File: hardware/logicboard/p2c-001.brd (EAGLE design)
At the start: 91 x 55 mm, 49 parts, among them IC1 74LS07N, J1 POWER_JACKSLT, J2 RLY, J3 DISP, J4 PWR, J5 DIN5, J6 DIN5, J7 Qwiic, K1 G5V1, Q1 220mA/50V/3.5Ω, Q2 220mA/50V/3.5Ω, SW1 A6A-16R, T1 2SC1815, U1 DS18B20

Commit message: Fixed value of capacitor.
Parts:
- C2: value 0.47u -> 0.33u
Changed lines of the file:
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@@
 <?xml version="1.0" encoding="utf-8"?>
 <!DOCTYPE eagle SYSTEM "eagle.dtd">
-<eagle version="9.5.2">
+<eagle version="9.6.1">
 <drawing>
 <settings>
@@
 <attribute name="VALUE" x="30.222" y="10.333" size="1.27" layer="27" ratio="10"/>
 </element>
-<element name="C2" library="rcl" library_urn="urn:adsk.eagle:library:334" package="C050-024X044" package3d_urn="urn:adsk.eagle:package:23643/1" value="0.47u" x="24" y="13" smashed="yes">
+<element name="C2" library="rcl" library_urn="urn:adsk.eagle:library:334" package="C050-024X044" package3d_urn="urn:adsk.eagle:package:23643/1" value="0.33u" x="24" y="13" smashed="yes">
 <attribute name="NAME" x="20.5" y="13" size="1" layer="25" ratio="10" rot="R90" align="bottom-center"/>
 <attribute name="POPULARITY" value="33" x="24" y="13" size="1.778" layer="27" display="off"/>

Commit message: Renamed J7 to JQ1.
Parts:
- renumbered J7 to JQ1
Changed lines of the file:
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@@
 <?xml version="1.0" encoding="utf-8"?>
 <!DOCTYPE eagle SYSTEM "eagle.dtd">
-<eagle version="9.6.1">
+<eagle version="9.5.2">
 <drawing>
 <settings>
@@
 <attribute name="VALUE" x="61.8664" y="30.2286" size="0.9906" layer="27" ratio="10"/>
 </element>
-<element name="J7" library="SparkFun-Connectors" library_urn="urn:adsk.eagle:library:513" package="1X04_1MM_RA" package3d_urn="urn:adsk.eagle:package:38096/1" value="Qwiic" x="45.5" y="49" smashed="yes" rot="MR180">
+<element name="JQ1" library="SparkFun-Connectors" library_urn="urn:adsk.eagle:library:513" package="1X04_1MM_RA" package3d_urn="urn:adsk.eagle:package:38096/1" value="Qwiic" x="45.5" y="49" smashed="yes" rot="MR180">
 <attribute name="NAME" x="45.5" y="47" size="1" layer="26" ratio="20" rot="MR0" align="bottom-center"/>
 <attribute name="VALUE" x="43.849" y="52.302" size="0.6096" layer="28" font="vector" ratio="20" rot="MR180"/>
@@
 <contactref element="C5" pad="2"/>
 <contactref element="C6" pad="2"/>
-<contactref element="J7" pad="1"/>
+<contactref element="JQ1" pad="1"/>
 <contactref element="JP1" pad="1"/>
 <contactref element="L1" pad="K"/>
@@
 <contactref element="Q1" pad="1"/>
 <contactref element="RC2" pad="2"/>
-<contactref element="J7" pad="2"/>
+<contactref element="JQ1" pad="2"/>
 <wire x1="41.4528" y1="41.6814" x2="41.4528" y2="41.0718" width="0.3048" layer="16"/>
 <wire x1="40.6908" y1="42.4434" x2="41.4528" y2="41.6814" width="0.3048" layer="16"/>
@@
 <contactref element="RC4" pad="1"/>
 <contactref element="Q2" pad="2"/>
-<contactref element="J7" pad="3"/>
+<contactref element="JQ1" pad="3"/>
 <contactref element="RZ2" pad="2"/>
 <wire x1="42.9006" y1="41.529" x2="41.529" y2="42.9006" width="0.1524" layer="16"/>
@@
 <contactref element="RC2" pad="1"/>
 <contactref element="Q1" pad="2"/>
-<contactref element="J7" pad="4"/>
+<contactref element="JQ1" pad="4"/>
 <contactref element="RZ1" pad="2"/>
 <wire x1="47.0916" y1="41.0718" x2="49.4538" y2="41.0718" width="0.1524" layer="16"/>

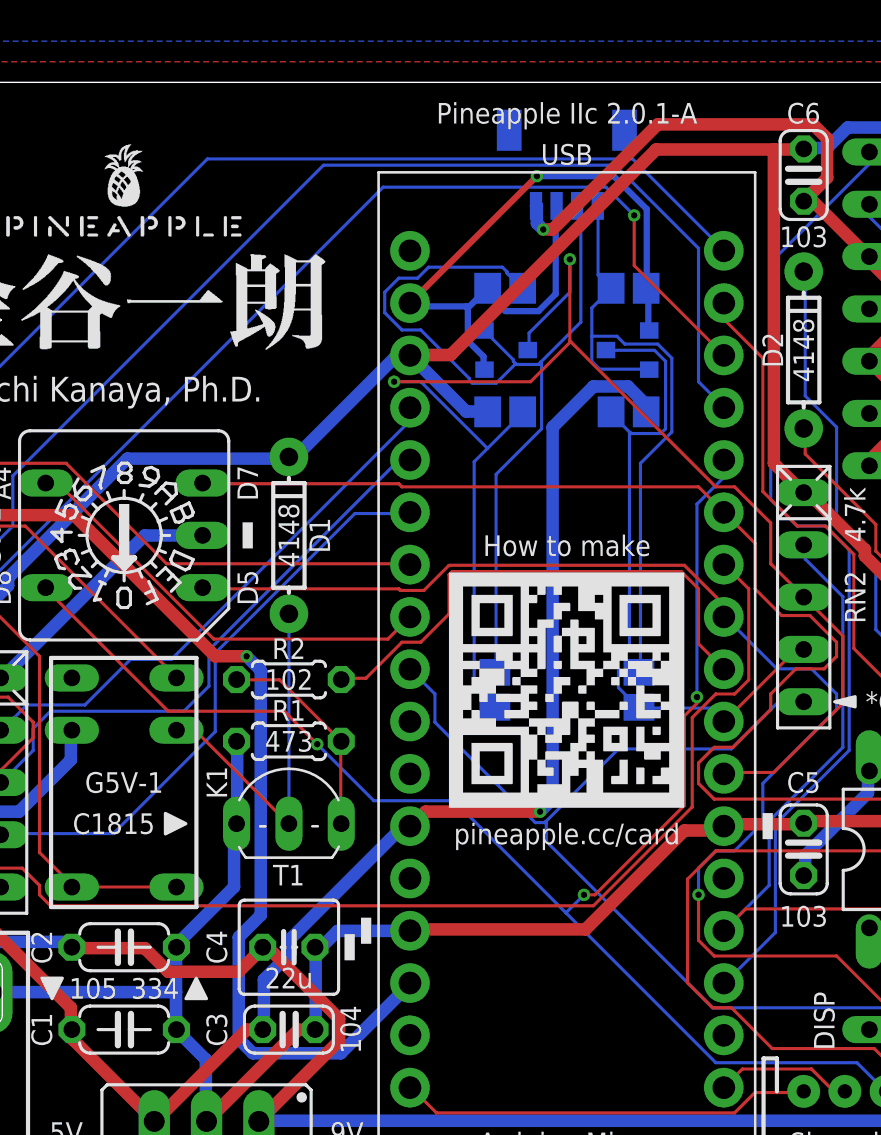
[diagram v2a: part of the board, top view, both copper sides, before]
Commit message: Fixed capacitance (again).
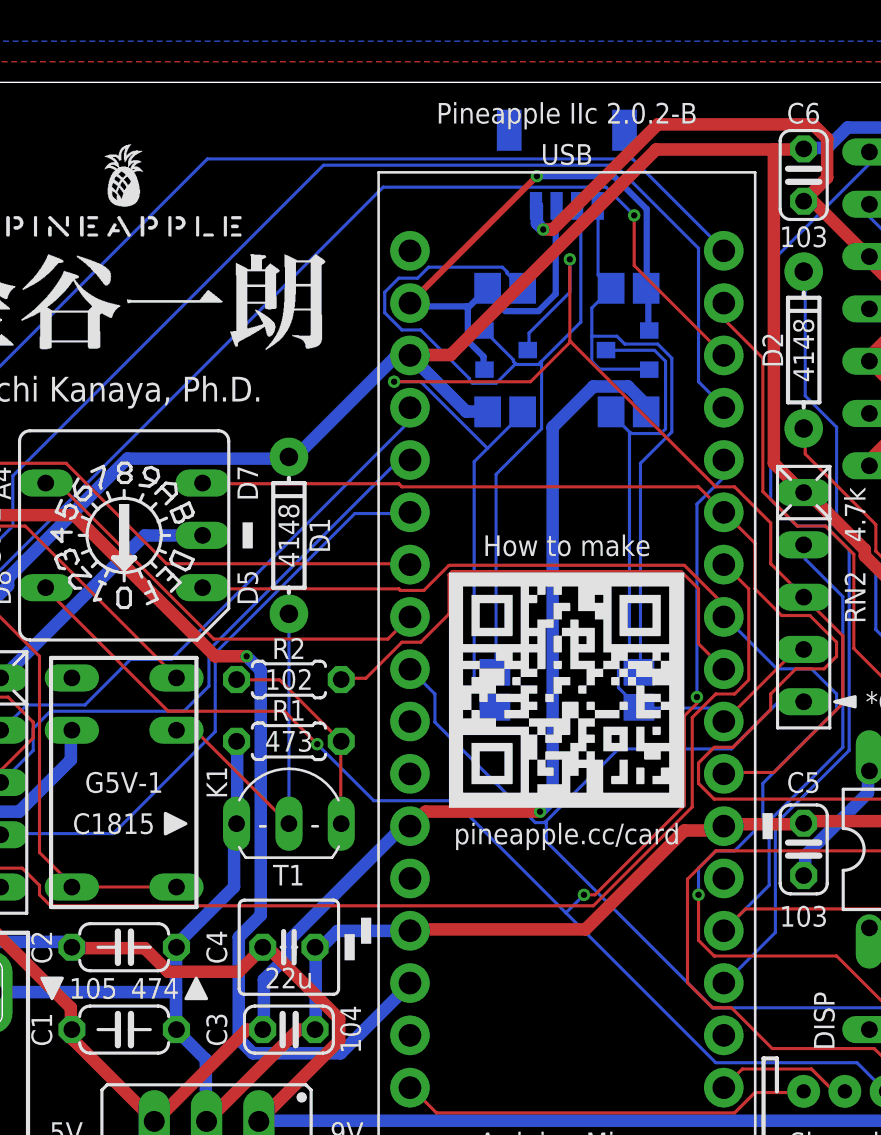
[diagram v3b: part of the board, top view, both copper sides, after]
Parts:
- C2: value 0.33u -> 0.47u
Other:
- board text added: "474"
- board text added: "Pineapple IIc 2.0.2-B"
- board text removed: "334"
- board text removed: "Pineapple IIc 2.0.1-A"
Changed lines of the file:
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@@
 <vertex x="40" y="20"/>
 </polygon>
-<text x="45.5" y="53" size="1" layer="25" align="bottom-center">Pineapple IIc 2.0.1-A</text>
+<text x="45.5" y="53" size="1" layer="25" align="bottom-center">Pineapple IIc 2.0.2-B</text>
 <text x="5" y="8" size="1" layer="25" align="center-left">GND</text>
 <text x="45.5" y="3" size="1" layer="25" align="bottom-center">Arduino Micro</text>
@@
 <text x="34" y="1" size="1" layer="25">7805</text>
 <text x="32" y="11" size="1" layer="25" align="bottom-center">22u</text>
-<text x="25.5" y="11" size="1" layer="25" align="center">334</text>
+<text x="25.5" y="11" size="1" layer="25" align="center">474</text>
 <polygon width="0.15" layer="21">
 <vertex x="20" y="11.5"/>
@@
 <attribute name="VALUE" x="30.222" y="10.333" size="1.27" layer="27" ratio="10"/>
 </element>
-<element name="C2" library="rcl" library_urn="urn:adsk.eagle:library:334" package="C050-024X044" package3d_urn="urn:adsk.eagle:package:23643/1" value="0.33u" x="24" y="13" smashed="yes">
+<element name="C2" library="rcl" library_urn="urn:adsk.eagle:library:334" package="C050-024X044" package3d_urn="urn:adsk.eagle:package:23643/1" value="0.47u" x="24" y="13" smashed="yes">
 <attribute name="NAME" x="20.5" y="13" size="1" layer="25" ratio="10" rot="R90" align="bottom-center"/>
 <attribute name="POPULARITY" value="33" x="24" y="13" size="1.778" layer="27" display="off"/>

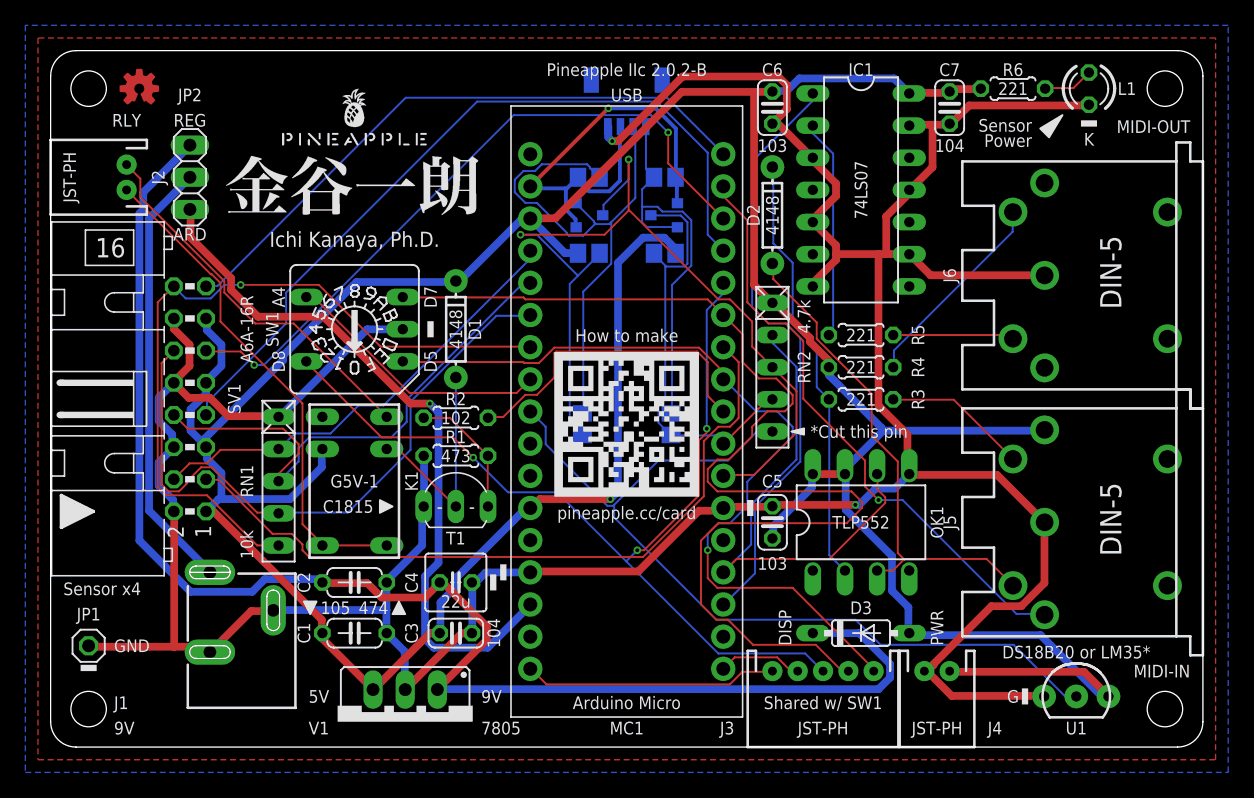
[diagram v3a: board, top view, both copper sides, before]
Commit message: Added bogopins to connect the logicboard and the groveboard.
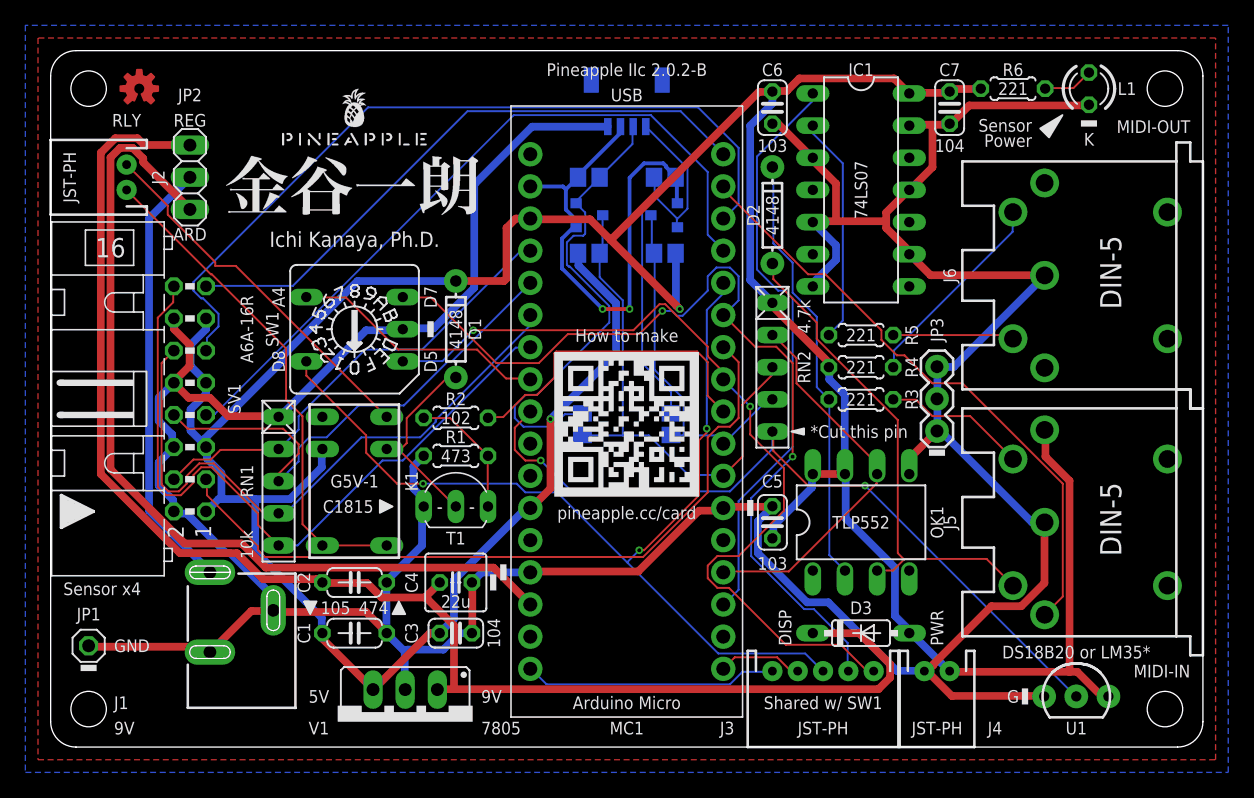
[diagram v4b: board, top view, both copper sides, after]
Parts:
- added JP3: GNDPINS, SparkFun-Connectors:1X03
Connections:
- net GND: now also JP3.1, JP3.2, JP3.3
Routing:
- net SDA: track 71.1 -> 40.9 mm, vias 2 -> 0
- net DISP2: track 92.2 -> 73.1 mm, vias 0 -> 2
- net GND: track 286.0 -> 305.0 mm, vias 2 -> 0
- net +9V: track 56.5 -> 71.0 mm, vias 1 -> 0
- net RX: track 39.6 -> 30.2 mm
- net DTCT3: track 54.3 -> 63.0 mm, vias 2 -> 0
- net SDA3V3: track 44.9 -> 37.4 mm
- net THS: track 68.8 -> 61.6 mm, vias 0 -> 2
- net VCC: track 283.5 -> 278.1 mm, vias 1 -> 2
- net SCL: track 33.4 -> 28.2 mm
- net VDD: track 36.9 -> 40.7 mm, vias 1 -> 2
- net DTCT2: track 61.8 -> 58.0 mm
- net ANLG4: track 58.9 -> 56.9 mm, vias 1 -> 0
- net DISP1: track 65.8 -> 67.8 mm, vias 1 -> 2
- net DISP3: track 76.4 -> 77.8 mm
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
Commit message: Now the sensor output LED is connected to D11. (Following the new design of Pineapple II.)
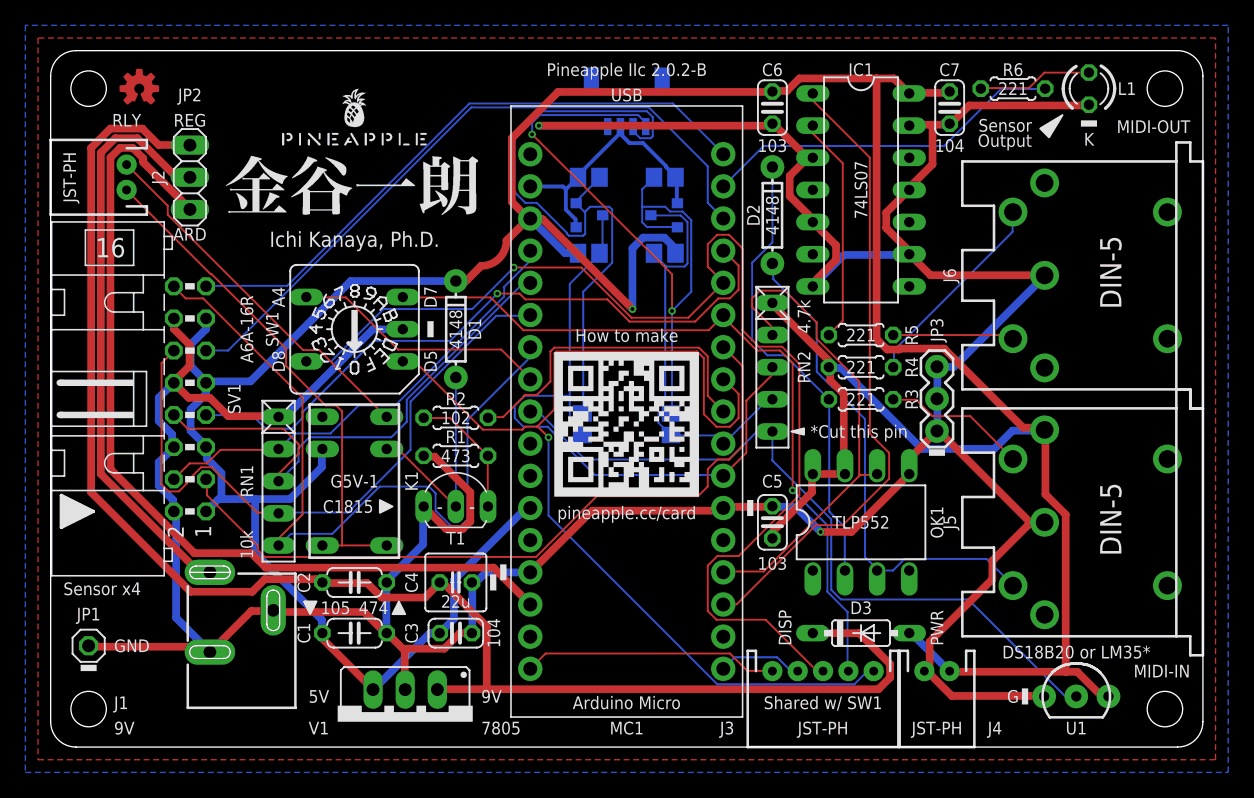
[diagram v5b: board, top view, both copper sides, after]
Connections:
- removed net AUX: J5.3, U$2.P$2
- removed net LED0A: L1.A, R6.1
- new net LED1: R6.1, U$2.P$2
- new net N$1: L1.A, R6.2
- net VCC: no longer R6.2
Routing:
- net AUX: track 48.1 -> 0.00 mm
- net LED1: track 0.00 -> 28.6 mm
- net SCL3V3: track 32.3 -> 56.4 mm, vias 0 -> 2
- net VDD: track 40.7 -> 21.6 mm, vias 2 -> 0
- net SDA3V3: track 37.4 -> 52.3 mm
- net DISP3: track 77.8 -> 92.5 mm, vias 3 -> 1
- net DISP1: track 67.8 -> 81.9 mm, vias 2 -> 1
- net DISP2: track 73.1 -> 60.2 mm, vias 2 -> 1
- net SDA: track 40.9 -> 53.2 mm
- net VIN: track 34.5 -> 46.0 mm
- net VCC: track 278.1 -> 287.8 mm, vias 2 -> 1
- net N$1: track 0.00 -> 9.06 mm
- net DTCT3: track 63.0 -> 54.1 mm
- net RX: track 30.2 -> 38.8 mm
- net VREGIN: track 117.0 -> 122.9 mm
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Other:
- board text added: "Output"
- board text removed: "3: D11"
- board text removed: "Power"

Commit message: New display connector.
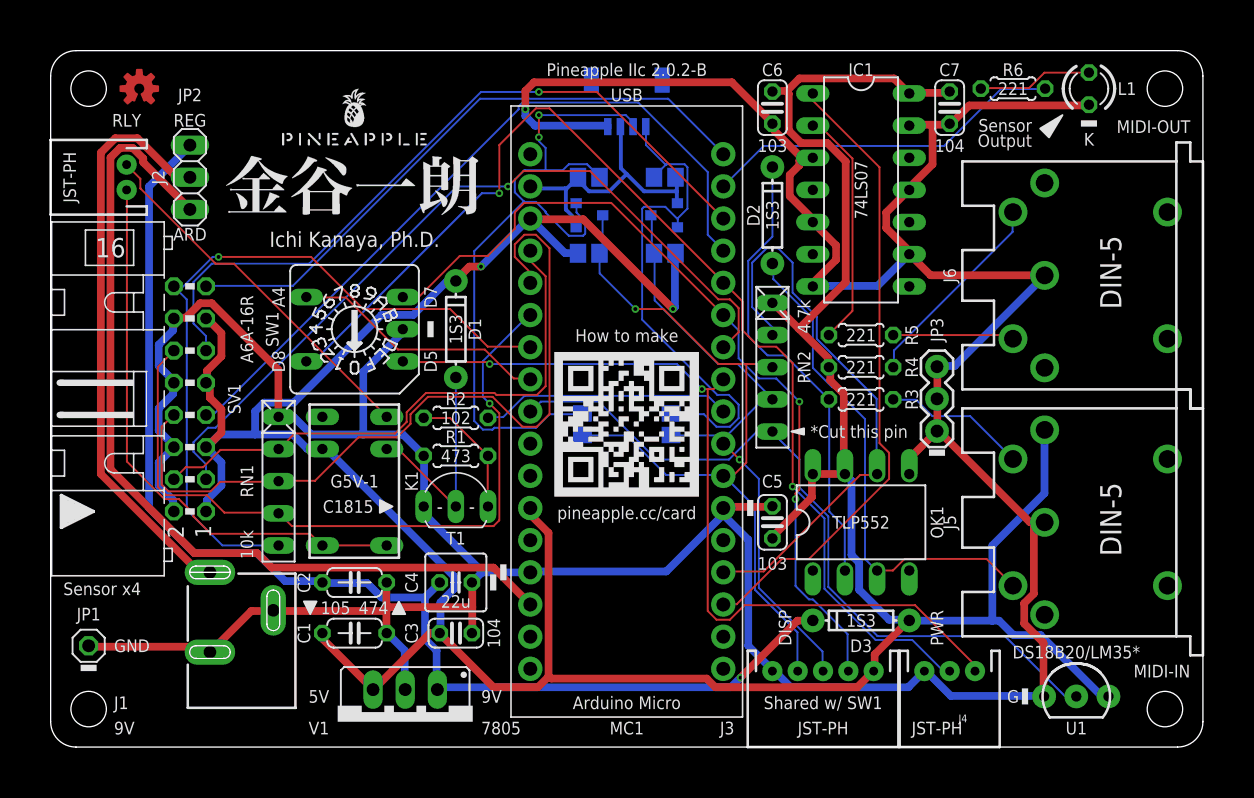
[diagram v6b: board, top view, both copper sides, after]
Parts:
- D3: value Shottky D. -> (none); device diode:DO35-7 -> SparkFun-DiscreteSemi:DIODE-1N4148
- J3: value DISP -> I2C
- J4: value PWR -> (none); device SparkFun-Connectors:JST-2-PTH -> SparkFun-Connectors:JST-3-PTH
- moved D3 1.00 mm to (64.0, 10.0), turned to 180 degrees
- moved J4 1.00 mm to (71.0, 6.00)
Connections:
- removed net DISP3: J3.3, SW1.8, U$2.P$5
- new net D7: J3.2, SW1.4, U$2.P$6
- net DISP1: now also J4.1; no longer J3.1
- net DISP2: now also J4.2, SW1.8, U$2.P$5; no longer J3.2, SW1.4, U$2.P$6
- net GND: now also J3.5, J4.3; no longer J4.2
- net MOSI: no longer J3.4
- net SCL: now also J3.3
- net SCLK: no longer J3.5
- net SDA: now also J3.4
- net VCC: now also J3.1; no longer J4.1
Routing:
- net DISP3: track 92.5 -> 0.00 mm, vias 1 -> 0
- net D7: track 0.00 -> 66.3 mm, vias 0 -> 2
- net DISP2: track 60.2 -> 90.1 mm, vias 1 -> 2
- net VREGIN: track 122.9 -> 95.9 mm, vias 0 -> 1
- net SCLK: track 20.2 -> 0.00 mm
- net ANLG2: track 42.4 -> 61.9 mm
- net SCL: track 33.4 -> 51.0 mm, vias 0 -> 1
- net GND: track 303.3 -> 319.0 mm, vias 2 -> 1
- net SCL3V3: track 56.4 -> 41.5 mm, vias 2 -> 0
- net DISP1: track 81.9 -> 68.4 mm, vias 1 -> 2
- net SDA: track 53.2 -> 61.8 mm, vias 0 -> 1
- net ANLG1: track 36.6 -> 44.2 mm
- net SDA3V3: track 52.3 -> 59.4 mm, vias 0 -> 2
- net MOSI: track 6.71 -> 0.00 mm
- net ANLG3: track 51.5 -> 58.1 mm, vias 0 -> 1
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- removed copper zone on layer 1, net GND
- removed copper zone on layer 16, net GND
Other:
- board text added: "1S3"
- board text added: "DISP1"
- board text added: "DISP2"
- board text added: "DS18B20/LM35*"
- board text added: "SCL"
- board text added: "SDA"
- board text removed: "4148"
- board text removed: "DS18B20 or LM35*"
- board text removed: "MOSI"
- board text removed: "SCLK"

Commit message: Looks good.
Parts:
- J4: value (none) -> DISP
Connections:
- removed net MOSI: U$2.P$17
- removed net SCLK: U$2.P$18
- net D7: now also J3.4; no longer J3.2
- net DISP1: now also J4.3; no longer J4.1
- net GND: now also J3.1, J4.1; no longer J3.5, J4.3
- net SDA: now also J3.2; no longer J3.4
- net VCC: now also J3.5; no longer J3.1, J5.1
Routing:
- net VCC: track 283.8 -> 252.6 mm, vias 2 -> 3
- net VREGIN: track 95.9 -> 112.7 mm, vias 1 -> 0
- net ANLG2: track 61.9 -> 45.6 mm, vias 0 -> 1
- net DISP2: track 90.1 -> 106.1 mm, vias 2 -> 1
- net DISP1: track 68.4 -> 83.5 mm, vias 2 -> 1
- net VIN: track 46.0 -> 34.5 mm
- net SCL: track 51.0 -> 57.5 mm, vias 1 -> 0
- net SDA: track 61.8 -> 67.8 mm, vias 1 -> 0
- net +9V: track 71.0 -> 76.4 mm
- net GND: track 319.0 -> 323.7 mm, vias 1 -> 0
- net DTCT3: track 58.0 -> 53.6 mm, vias 1 -> 0
- net N$4: track 29.3 -> 33.1 mm
- net SCL3V3: track 41.5 -> 45.3 mm, vias 0 -> 3
- net N$6: track 44.9 -> 42.3 mm, vias 0 -> 1
- net DTCT2: track 59.0 -> 57.2 mm, vias 0 -> 1
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- added copper zone on layer 1, net GND
- added copper zone on layer 16, net GND
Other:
- board text added: "GPIO"
- board text added: "MKR"
- board text removed: "1: Vcc"
- board text removed: "DISP"
- board text removed: "DISP1"
- board text removed: "DISP2"
- board text removed: "PWR"
- board text removed: "Shared w/ SW1"
